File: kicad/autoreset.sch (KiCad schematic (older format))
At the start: 5 parts, among them Q1 Q_NPN_BCE, Q2 Q_NPN_BCE

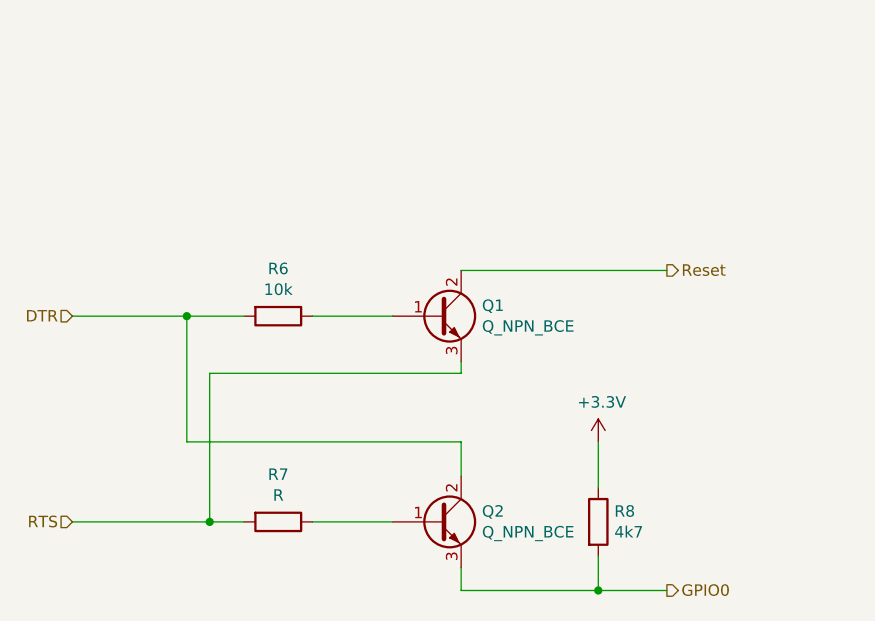
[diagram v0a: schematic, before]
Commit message: Pinliste und kleinere Verschönerungen, Transistor-Value, ...
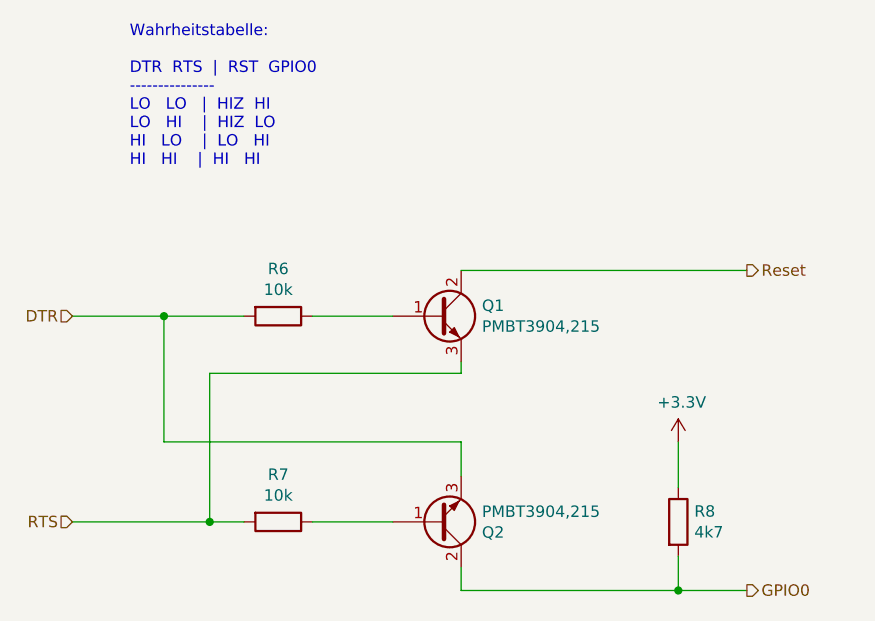
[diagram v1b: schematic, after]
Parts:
- Q1, Q2: value Q_NPN_BCE -> PMBT3904,215
- R7: value R -> 10k
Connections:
- net DTR: now also Q2.3 (E); no longer Q2.2 (C)
- net GPIO0: now also Q2.2 (C); no longer Q2.3 (E)
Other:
- note added: "Wahrheitstabelle:\n\nDTR RTS | RST GPIO0\n---------------\nLO LO | HIZ HI\nLO HI | HIZ LO\nHI LO | LO HI\nHI HI | HI HI"
- moved on the sheet: R8
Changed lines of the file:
@@
 $EndDescr
 Wire Wire Line
-	5300 4350 5900 4350
+	5300 4350 6250 4350
 Wire Wire Line
-	5900 3700 5900 3900
+	6250 3700 6250 3900
 $Comp
 L power:+3.3V #PWR?
 U 1 1 603FFF1B
-P 5900 3700
+P 6250 3700
 AR Path="/5F8674B3/603FFF1B" Ref="#PWR?"  Part="1"
 AR Path="/603FFF1B" Ref="#PWR?"  Part="1"
 AR Path="/603FCB6F/603FFF1B" Ref="#PWR06"  Part="1"
-F 0 "#PWR06" H 5900 3550 50  0001 C CNN
-F 1 "+3.3V" H 5915 3873 50  0000 C CNN
-F 2 "" H 5900 3700 50  0001 C CNN
-F 3 "" H 5900 3700 50  0001 C CNN
-	1    5900 3700
+F 0 "#PWR06" H 6250 3550 50  0001 C CNN
+F 1 "+3.3V" H 6265 3873 50  0000 C CNN
+F 2 "" H 6250 3700 50  0001 C CNN
+F 3 "" H 6250 3700 50  0001 C CNN
+	1    6250 3700
 	1    0    0    -1
 $EndComp
 Wire Wire Line
-	5900 4350 5900 4200
+	6250 4350 6250 4200
 Wire Wire Line
 	5300 4250 5300 4350
@@
 L Device:R R?
 U 1 1 603FFF23
-P 5900 4050
+P 6250 4050
 AR Path="/603FFF23" Ref="R?"  Part="1"
 AR Path="/603FCB6F/603FFF23" Ref="R8"  Part="1"
-F 0 "R8" H 5970 4096 50  0000 L CNN
-F 1 "4k7" H 5970 4005 50  0000 L CNN
-F 2 "Resistor_SMD:R_0603_1608Metric" V 5830 4050 50  0001 C CNN
-F 3 "" H 5900 4050 50  0001 C CNN
-	1    5900 4050
+F 0 "R8" H 6320 4096 50  0000 L CNN
+F 1 "4k7" H 6320 4005 50  0000 L CNN
+F 2 "Resistor_SMD:R_0603_1608Metric" V 6180 4050 50  0001 C CNN
+F 3 "" H 6250 4050 50  0001 C CNN
+	1    6250 4050
 	1    0    0    -1
 $EndComp
@@
 	4350 4050 4200 4050
 Wire Wire Line
-	4100 3150 4350 3150
+	4000 3150 4350 3150
 Wire Wire Line
-	4100 3700 4100 3150
+	4000 3700 4000 3150
 Wire Wire Line
-	5300 3700 4100 3700
+	5300 3700 4000 3700
 Wire Wire Line
 	5300 3850 5300 3700
@@
 AR Path="/603FCB6F/603FFF33" Ref="R7"  Part="1"
 F 0 "R7" V 4293 4050 50  0000 C CNN
-F 1 "R" V 4384 4050 50  0000 C CNN
+F 1 "10k" V 4384 4050 50  0000 C CNN
 F 2 "Resistor_SMD:R_0603_1608Metric" V 4430 4050 50  0001 C CNN
 F 3 "" H 4500 4050 50  0001 C CNN
@@
 AR Path="/603FCB6F/603FFF39" Ref="Q2"  Part="1"
 F 0 "Q2" H 5391 4096 50  0000 L CNN
-F 1 "Q_NPN_BCE" H 5391 4005 50  0000 L CNN
+F 1 "PMBT3904,215" H 5391 4005 50  0000 L CNN
 F 2 "Package_TO_SOT_SMD:SOT-23" H 5400 4150 50  0001 C CNN
 F 3 "~" H 5200 4050 50  0001 C CNN
 	1    5200 4050
-	1    0    0    -1
+	1    0    0    1
 $EndComp
 $Comp
@@
 AR Path="/603FCB6F/603FFF3F" Ref="Q1"  Part="1"
 F 0 "Q1" H 5391 3196 50  0000 L CNN
-F 1 "Q_NPN_BCE" H 5391 3105 50  0000 L CNN
+F 1 "PMBT3904,215" H 5391 3105 50  0000 L CNN
 F 2 "Package_TO_SOT_SMD:SOT-23" H 5400 3250 50  0001 C CNN
 F 3 "~" H 5200 3150 50  0001 C CNN
@@
 	1    0    0    -1
 $EndComp
-Text HLabel 6200 2950 2    50   Output ~ 0
+Text HLabel 6550 2950 2    50   Output ~ 0
 Reset
-Text HLabel 6200 4350 2    50   Output ~ 0
+Text HLabel 6550 4350 2    50   Output ~ 0
 GPIO0
 Text HLabel 3600 3150 0    50   Input ~ 0
@@
 $EndComp
 Wire Wire Line
-	6200 4350 5900 4350
-Connection ~ 5900 4350
+	6550 4350 6250 4350
+Connection ~ 6250 4350
 Wire Wire Line
 	3600 4050 4200 4050
 Connection ~ 4200 4050
 Wire Wire Line
-	3600 3150 4100 3150
-Connection ~ 4100 3150
+	3600 3150 4000 3150
+Connection ~ 4000 3150
 Wire Wire Line
-	6200 2950 5300 2950
+	6550 2950 5300 2950
+Text Notes 3850 2500 0    50   ~ 0
+Wahrheitstabelle:\n\nDTR  RTS  |  RST  GPIO0\n---------------\nLO   LO   |  HIZ  HI\nLO   HI    |  HIZ  LO\nHI   LO    |  LO   HI\nHI   HI    |  HI   HI
 $EndSCHEMATC

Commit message: BOM fertig eingepflegt
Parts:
- Q1, Q2: DistOrderNr (none) -> C8667; Distributor (none) -> LCSC; ManPartNr (none) -> PMBT3904,215; Manufacturer (none) -> Nexperia; Notes (none) -> NPN 200mA 40V 250mW SOT-23; PriceEUR (none) -> 0.0109; PriceForQty (none) -> 50
- R6, R7: DistOrderNr (none) -> C103210; Distributor (none) -> LCSC; ManPartNr (none) -> RTT03103JTP; Manufacturer (none) -> RALEC; Notes (none) -> 10kΩ ±5% 0.1W ±100ppm/℃; PriceEUR (none) -> 0.0015; PriceForQty (none) -> 100
- R8: DistOrderNr (none) -> C103662; Distributor (none) -> LCSC; ManPartNr (none) -> RTT03472JTP; Manufacturer (none) -> RALEC; Notes (none) -> 4.7kΩ ±5% 0.1W ±100ppm/K; PriceEUR (none) -> 0.0015; PriceForQty (none) -> 100
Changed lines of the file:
@@
 F 2 "Resistor_SMD:R_0603_1608Metric" V 6180 4050 50  0001 C CNN
 F 3 "" H 6250 4050 50  0001 C CNN
+F 4 "C103662" H 6250 4050 50  0001 C CNN "DistOrderNr"
+F 5 "LCSC" H 6250 4050 50  0001 C CNN "Distributor"
+F 6 " RTT03472JTP" H 6250 4050 50  0001 C CNN "ManPartNr"
+F 7 "RALEC" H 6250 4050 50  0001 C CNN "Manufacturer"
+F 8 "4.7kΩ ±5% 0.1W ±100ppm/K" H 6250 4050 50  0001 C CNN "Notes"
+F 9 "0.0015" H 6250 4050 50  0001 C CNN "PriceEUR"
+F 10 "100" H 6250 4050 50  0001 C CNN "PriceForQty"
 	1    6250 4050
 	1    0    0    -1
@@
 F 2 "Resistor_SMD:R_0603_1608Metric" V 4430 4050 50  0001 C CNN
 F 3 "" H 4500 4050 50  0001 C CNN
+F 4 "C103210" H 4500 4050 50  0001 C CNN "DistOrderNr"
+F 5 "LCSC" H 4500 4050 50  0001 C CNN "Distributor"
+F 6 "RTT03103JTP" H 4500 4050 50  0001 C CNN "ManPartNr"
+F 7 "RALEC" H 4500 4050 50  0001 C CNN "Manufacturer"
+F 8 "10kΩ ±5% 0.1W ±100ppm/℃" H 4500 4050 50  0001 C CNN "Notes"
+F 9 "0.0015" H 4500 4050 50  0001 C CNN "PriceEUR"
+F 10 "100" H 4500 4050 50  0001 C CNN "PriceForQty"
 	1    4500 4050
 	0    1    1    0
@@
 F 2 "Package_TO_SOT_SMD:SOT-23" H 5400 4150 50  0001 C CNN
 F 3 "~" H 5200 4050 50  0001 C CNN
+F 4 "C8667" H 5200 4050 50  0001 C CNN "DistOrderNr"
+F 5 "LCSC" H 5200 4050 50  0001 C CNN "Distributor"
+F 6 "PMBT3904,215" H 5200 4050 50  0001 C CNN "ManPartNr"
+F 7 "Nexperia" H 5200 4050 50  0001 C CNN "Manufacturer"
+F 8 "NPN 200mA 40V 250mW SOT-23" H 5200 4050 50  0001 C CNN "Notes"
+F 9 "0.0109" H 5200 4050 50  0001 C CNN "PriceEUR"
+F 10 "50" H 5200 4050 50  0001 C CNN "PriceForQty"
 	1    5200 4050
 	1    0    0    1
@@
 F 2 "Package_TO_SOT_SMD:SOT-23" H 5400 3250 50  0001 C CNN
 F 3 "~" H 5200 3150 50  0001 C CNN
+F 4 "C8667" H 5200 3150 50  0001 C CNN "DistOrderNr"
+F 5 "LCSC" H 5200 3150 50  0001 C CNN "Distributor"
+F 6 "PMBT3904,215" H 5200 3150 50  0001 C CNN "ManPartNr"
+F 7 "Nexperia" H 5200 3150 50  0001 C CNN "Manufacturer"
+F 8 "NPN 200mA 40V 250mW SOT-23" H 5200 3150 50  0001 C CNN "Notes"
+F 9 "0.0109" H 5200 3150 50  0001 C CNN "PriceEUR"
+F 10 "50" H 5200 3150 50  0001 C CNN "PriceForQty"
 	1    5200 3150
 	1    0    0    -1
@@
 F 2 "Resistor_SMD:R_0603_1608Metric" V 4430 3150 50  0001 C CNN
 F 3 "" H 4500 3150 50  0001 C CNN
+F 4 "C103210" H 4500 3150 50  0001 C CNN "DistOrderNr"
+F 5 "LCSC" H 4500 3150 50  0001 C CNN "Distributor"
+F 6 "RTT03103JTP" H 4500 3150 50  0001 C CNN "ManPartNr"
+F 7 "RALEC" H 4500 3150 50  0001 C CNN "Manufacturer"
+F 8 "10kΩ ±5% 0.1W ±100ppm/℃" H 4500 3150 50  0001 C CNN "Notes"
+F 9 "0.0015" H 4500 3150 50  0001 C CNN "PriceEUR"
+F 10 "100" H 4500 3150 50  0001 C CNN "PriceForQty"
 	1    4500 3150
 	0    1    1    0

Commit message: Schaltplanänderungen für v20.0.3 eingepflegt
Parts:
- Q1, Q2: symbol Device:Q_NPN_BCE -> Device:Q_NPN_BEC
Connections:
- net DTR: now also Q2.2 (E); no longer Q2.3 (E)
- net GPIO0: now also Q2.3 (C); no longer Q2.2 (C)
- net RTS: now also Q1.2 (E); no longer Q1.3 (E)
- net Reset: now also Q1.3 (C); no longer Q1.2 (C)
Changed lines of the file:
@@
 Sheet 3 5
 Title "Gamearino"
-Date "2021-04-29"
-Rev "V0.0.2"
+Date "2021-05-11"
+Rev "V20.0.3"
 Comp "HTL-Steyr"
 Comment1 "4ABHEL, 2020/2021"
@@
 $EndComp
 $Comp
-L Device:Q_NPN_BCE Q?
+L Device:Q_NPN_BEC Q?
 U 1 1 603FFF39
 P 5200 4050
@@
 $EndComp
 $Comp
-L Device:Q_NPN_BCE Q?
+L Device:Q_NPN_BEC Q?
 U 1 1 603FFF3F
 P 5200 3150

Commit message: Layoutbugfixes, v20.0.3 fertig, CAM-Daten
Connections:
- net Reset renamed ~RESET
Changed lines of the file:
@@
 $EndComp
 Text HLabel 6550 2950 2    50   Output ~ 0
-Reset
+~RESET
 Text HLabel 6550 4350 2    50   Output ~ 0
 GPIO0
